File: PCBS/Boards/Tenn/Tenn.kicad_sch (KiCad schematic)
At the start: 25 parts, among them J1 Conn_01x02_Socket, J12 Conn_01x04_Female, J13 Conn_01x03_Male, J14 Conn_01x03_Male, J15 Conn_01x03_Male, J16 Conn_01x02_Male, J17 Conn_01x02_Male, J18 Conn_01x30_Pin, SW2 SW_Push, SW3 SW_Push, SW4 SW_SPDT, U1 L7805, U2 DRV8871DDA, U3 DRV8871DDA

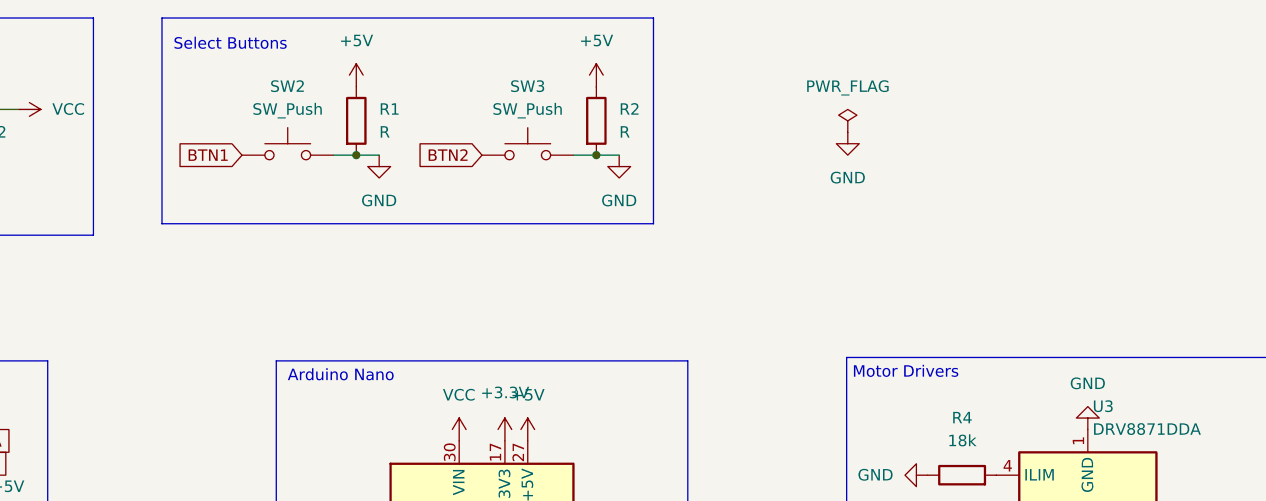
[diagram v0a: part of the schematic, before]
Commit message: updates tenn pcb, redesign to rev 2.2, fixed problem with button not working
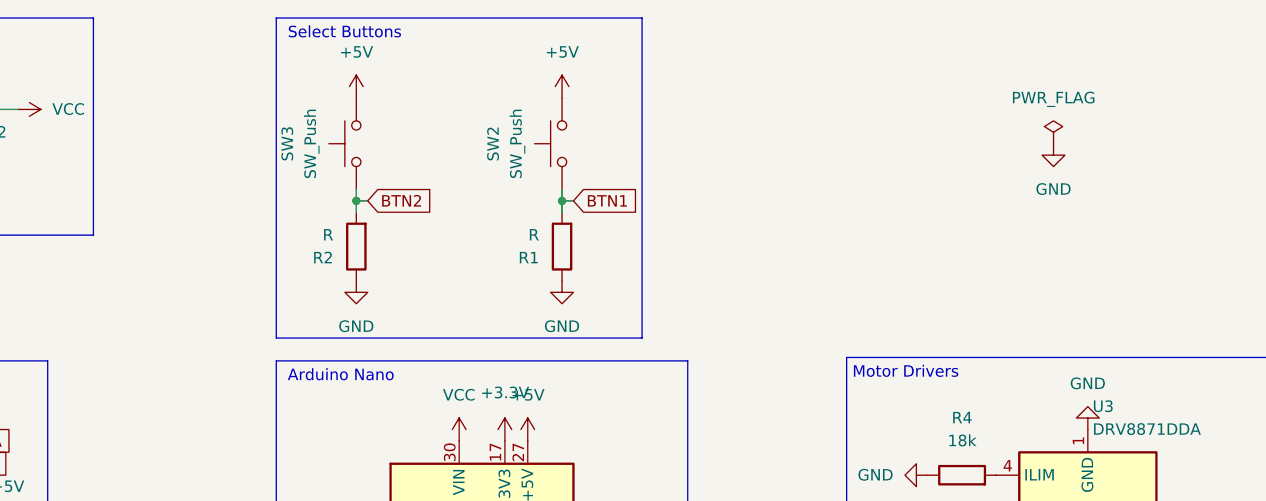
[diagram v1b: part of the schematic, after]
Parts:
- C5, C6: footprint Capacitor_Tantalum_SMD:CP_EIA-7343-31_Kemet-D_Pad2.25x2.55mm_HandSolder -> Capacitor_SMD:C_0805_2012Metric_Pad1.18x1.45mm_HandSolder
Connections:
- net +5V: now also SW2.2, SW3.2; no longer R1.1, R2.1
- net BTN1: now also R1.2
- net BTN2: now also R2.2
- net GND: now also R1.1, R2.1; no longer R1.2, R2.2, SW2.2, SW3.2
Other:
- moved on the sheet: R1, R2, SW2, SW3

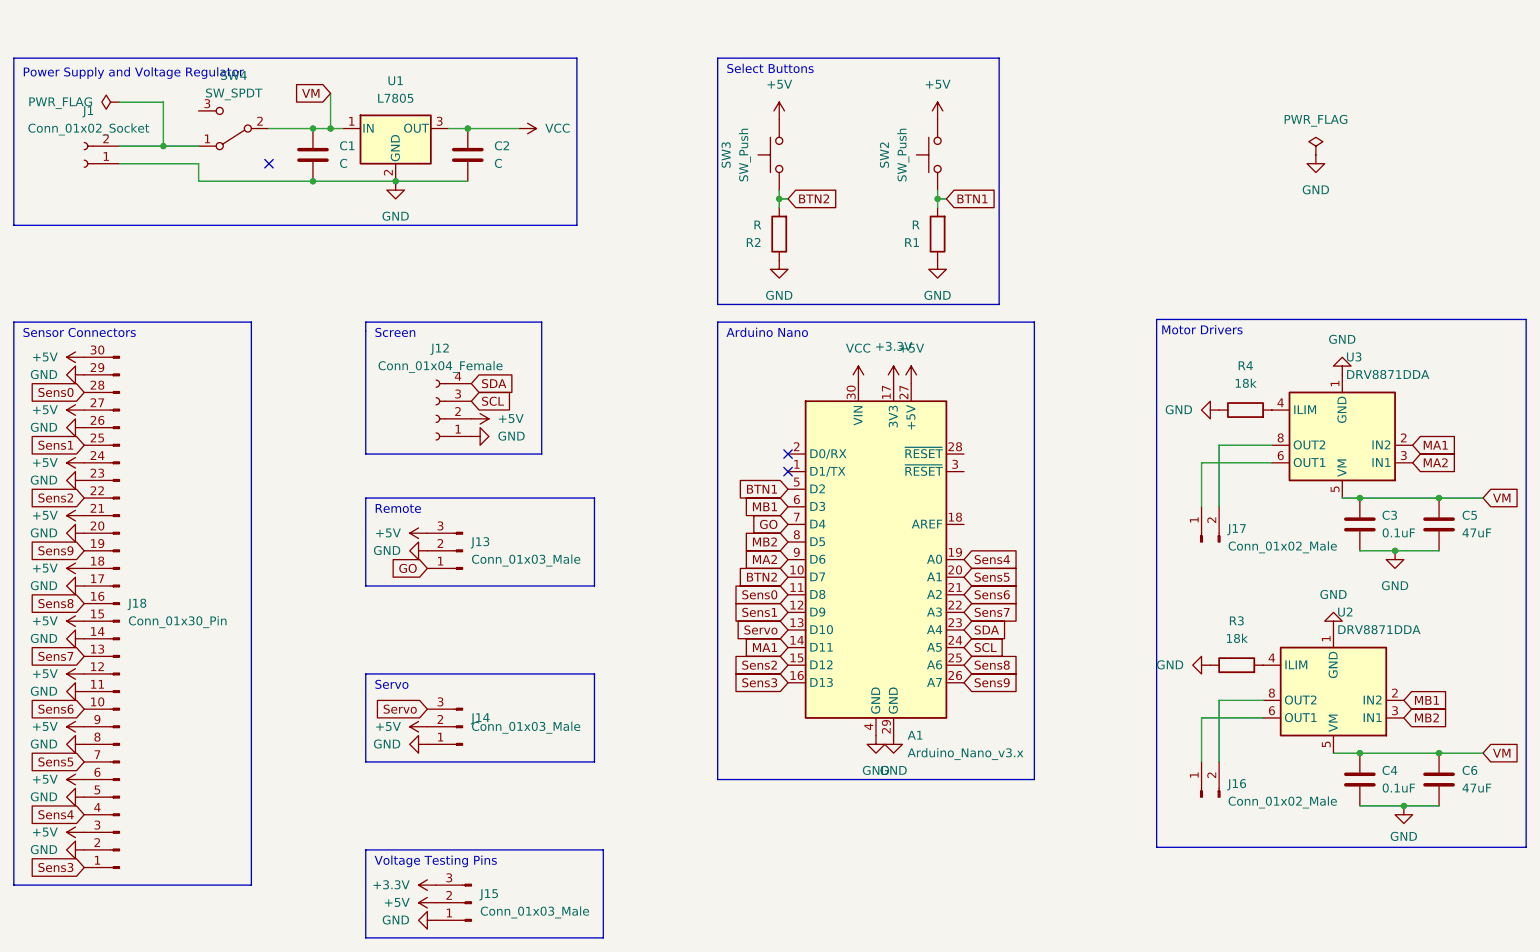
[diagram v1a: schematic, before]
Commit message: Updates Tenn, Rev 2.2 now fixes issues with the buttons not working correctly, the screen orientation, it also uses new components, supporting up to 6s theorical
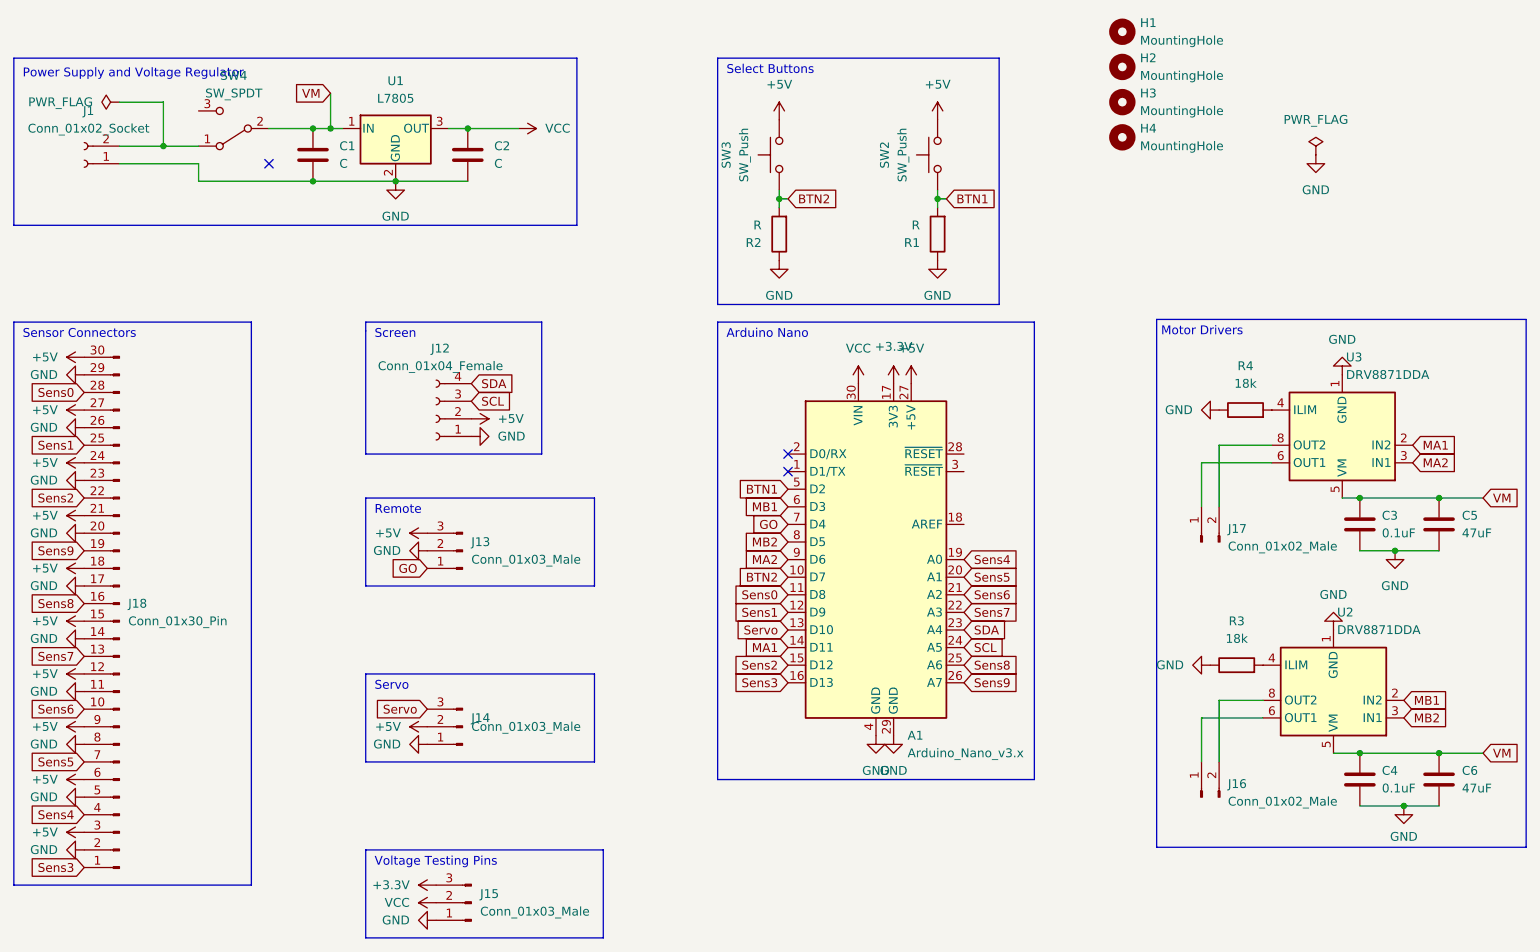
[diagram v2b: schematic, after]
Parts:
- added H1, H2, H3, H4: MountingHole, MountingHole:MountingHole_2.2mm_M2_ISO7380, symbol Mechanical:MountingHole
- SW4: footprint Button_Switch_SMD:SW_SPDT_PCM12 -> Button_Switch_THT:SW_Slide_SPDT_Straight_CK_OS102011MS2Q
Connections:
- net +5V: no longer J15.2 (Pin_2)
- net VCC: now also J15.2 (Pin_2)
